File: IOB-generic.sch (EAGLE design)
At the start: 19 parts, among them J1 RJ12/6, Q0 P-FET, Q1 P-FET, Q2 P-FET, Q3 P-FET

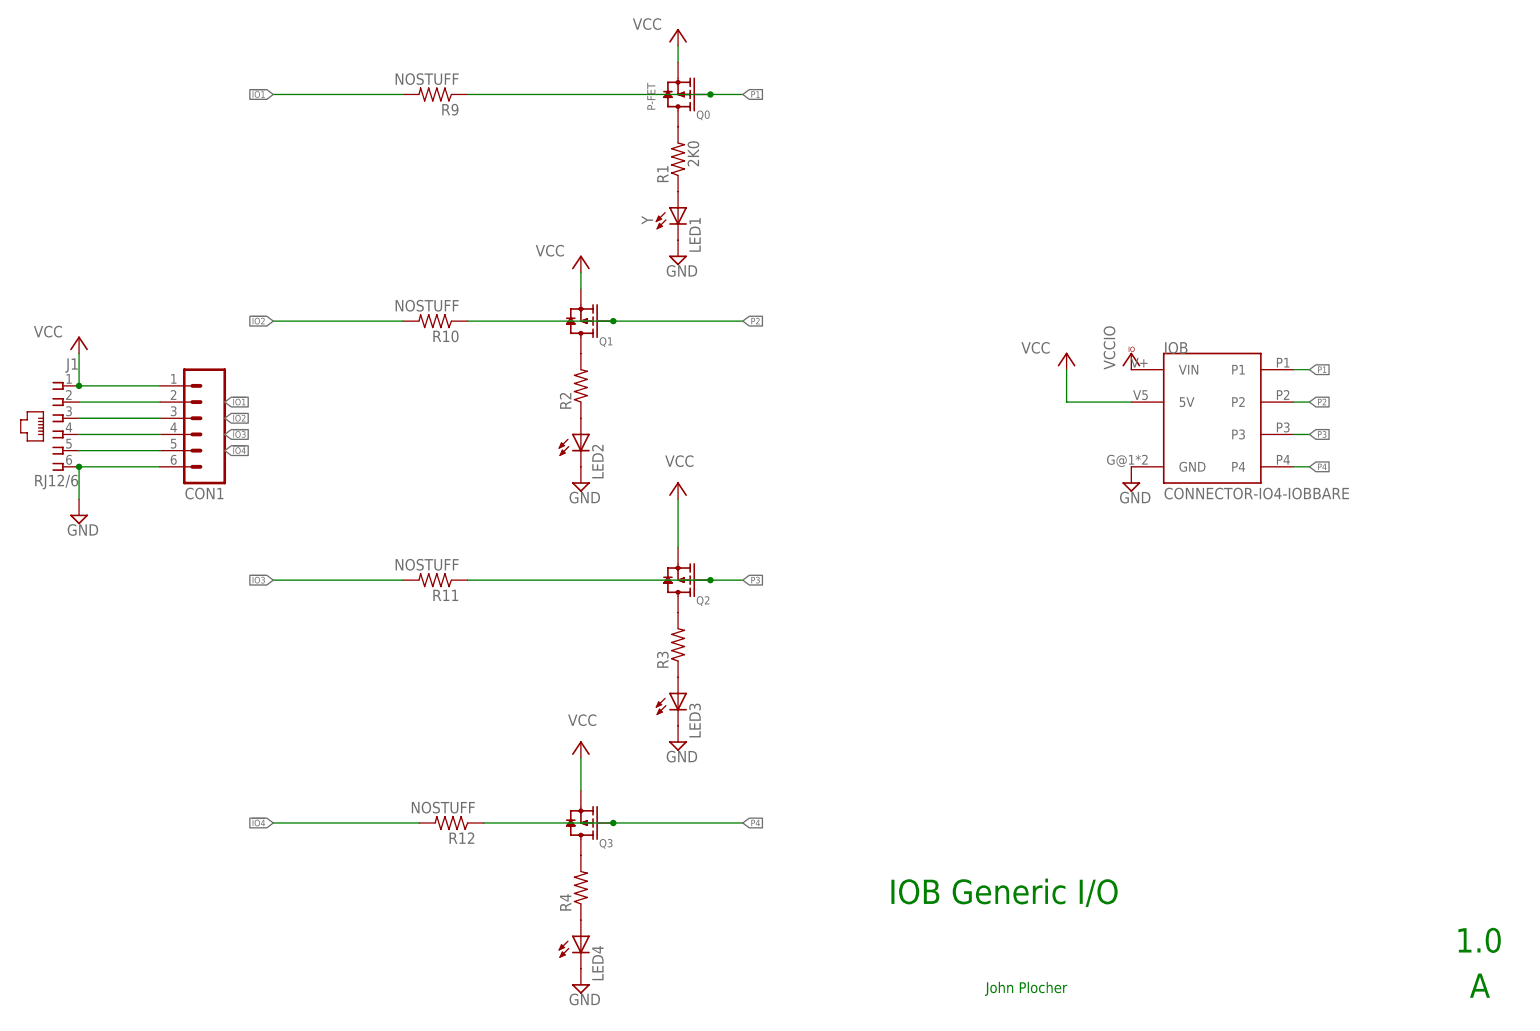
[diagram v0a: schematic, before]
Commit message: NEW IOB form factor
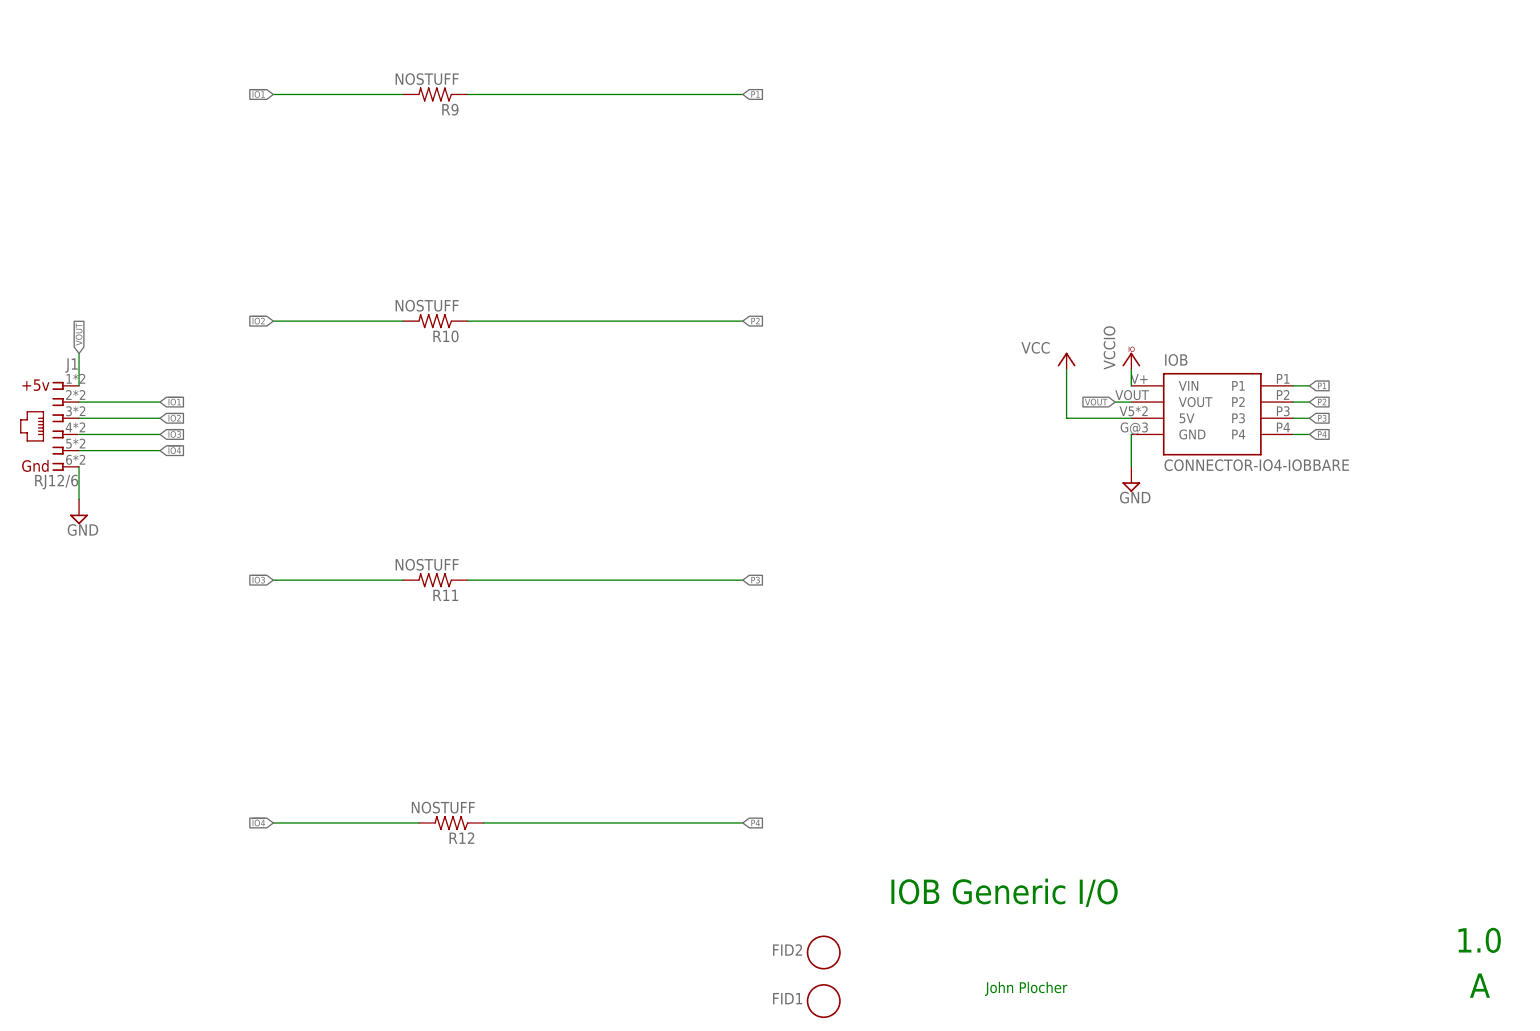
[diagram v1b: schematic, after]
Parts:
- removed CON1: (no value), SPCoast:CONNECTOR-M06LOCK
- removed LED1, LED2, LED3, LED4: Y, SPCoast:LED0603-LED
- removed Q0, Q1, Q2, Q3: P-FET, SPCoast:MOSFET-P-044021001
- removed R1, R2, R3, R4: 2K0, SPCoast:R0805-RES
- added FID1, FID2: FIDUCIAL, SPCoast:FIDUCIAL
- J1: device SPCoast:CONNECTOR-RJ25-6P6C -> SPCoast:CONNECTOR-IO4IPINS
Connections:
- removed net N$11: Q0.D, R1.2
- removed net N$2: LED1.A, R1.1
- removed net N$3: LED2.A, R2.1
- removed net N$30: Q1.D, R2.2
- removed net N$31: Q2.D, R3.2
- removed net N$32: Q3.D, R4.2
- removed net N$4: LED3.A, R3.1
- removed net N$5: LED4.A, R4.1
- new net VOUT: IOB.VOUT, J1.1
- net !IO1: no longer CON1.2
- net !IO2: no longer CON1.3
- net !IO3: no longer CON1.4
- net !IO4: no longer CON1.5
- net GND: no longer CON1.6, LED1.C, LED2.C, LED3.C, LED4.C
- net P1: no longer Q0.G
- net P2: no longer Q1.G
- net P3: no longer Q2.G
- net P4: no longer Q3.G
- net VCC: no longer CON1.1, J1.1, Q0.S, Q1.S, Q2.S, Q3.S

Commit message: updated version number
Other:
- note added: "2.0"
- note removed: "1.0"
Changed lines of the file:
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@@
 <plain>
 <text x="149.86" y="20.32" size="3.81" layer="91">IOB Generic I/O</text>
-<text x="238.76" y="12.7" size="3.81" layer="91">1.0</text>
+<text x="238.76" y="12.7" size="3.81" layer="91">2.0</text>
 <text x="241.046" y="5.588" size="3.81" layer="91">A</text>
 <text x="165.1" y="6.35" size="1.6764" layer="91" ratio="14">John Plocher</text>

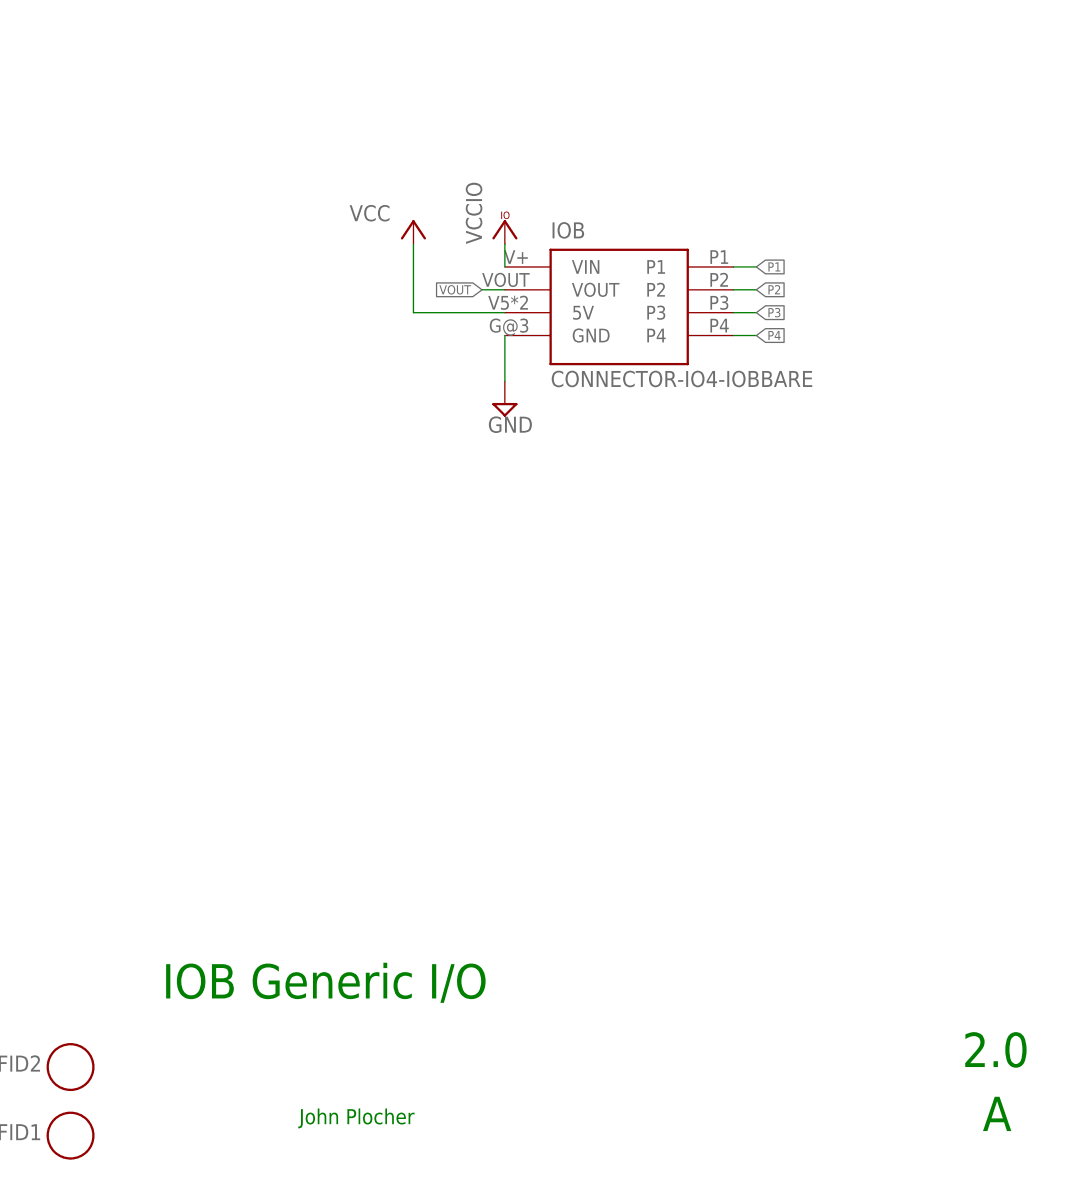
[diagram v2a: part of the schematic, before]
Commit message: silkscreen and top fill
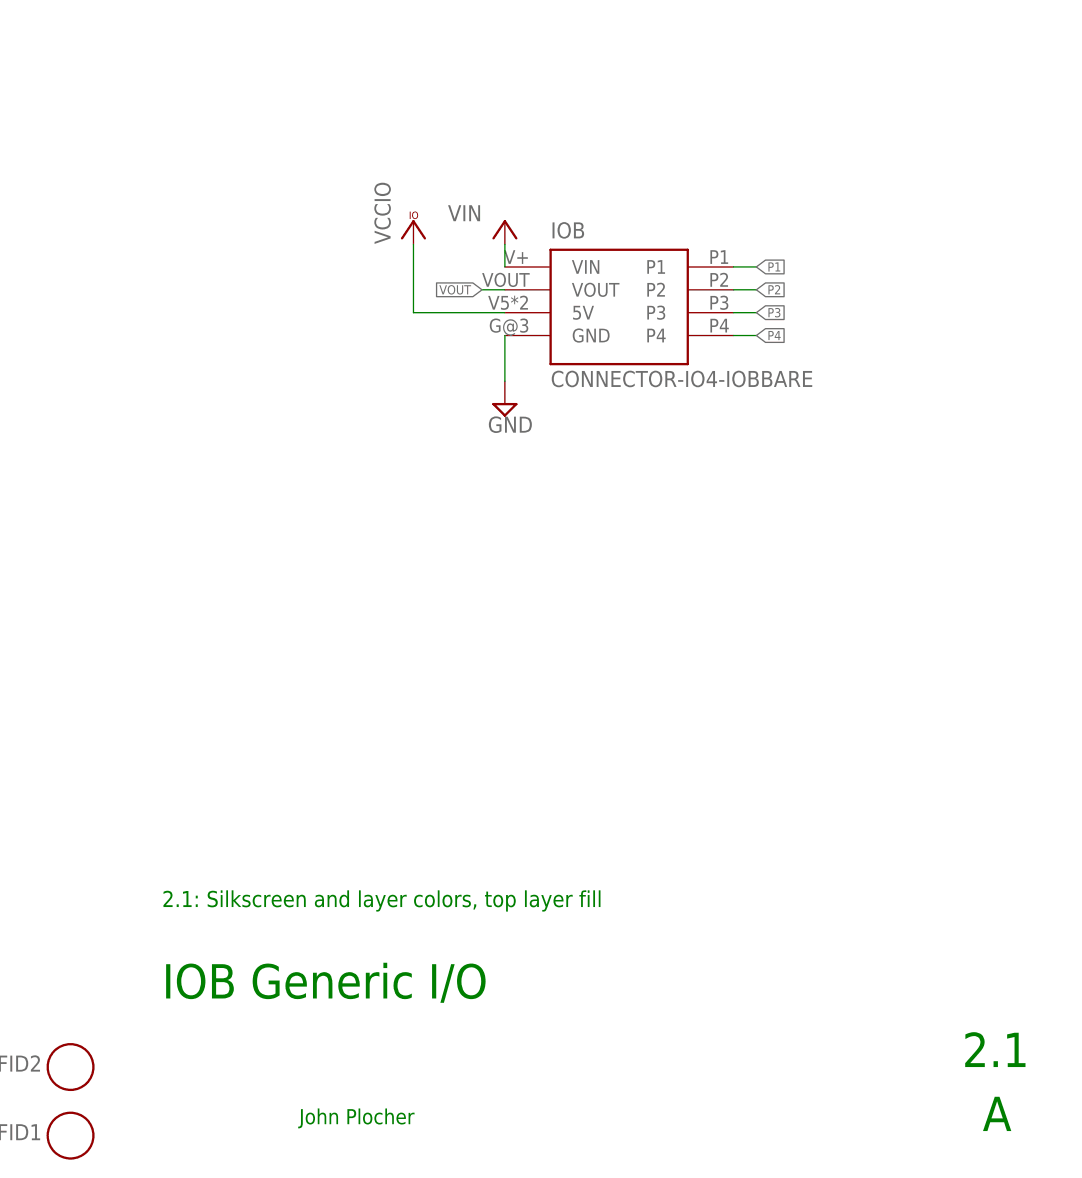
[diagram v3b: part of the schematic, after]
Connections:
- removed net VCC: IOB.5V
- new net VIN: IOB.VIN
- net VCCIO: now also IOB.5V; no longer IOB.VIN
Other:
- note added: "2.1"
- note added: "2.1: Silkscreen and layer colors, top layer fill"
- note removed: "2.0"
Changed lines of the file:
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@@
 <part name="IOB" library="SPCoast" deviceset="CONNECTOR-IO4-IOB" device="BARE"/>
 <part name="VCC3" library="SPCoast" deviceset="VCCIO" device=""/>
-<part name="P+7" library="supply1" deviceset="VCC" device=""/>
+<part name="VIN" library="supply1" deviceset="VCC" device="" value="VIN"/>
 <part name="V6" library="supply2" deviceset="GND" device=""/>
 <part name="R9" library="SPCoast" deviceset="R*" device="PTH04" value="NOSTUFF"/>
@@
 <plain>
 <text x="149.86" y="20.32" size="3.81" layer="91">IOB Generic I/O</text>
-<text x="238.76" y="12.7" size="3.81" layer="91">2.0</text>
+<text x="238.76" y="12.7" size="3.81" layer="91">2.1</text>
 <text x="241.046" y="5.588" size="3.81" layer="91">A</text>
 <text x="165.1" y="6.35" size="1.6764" layer="91" ratio="14">John Plocher</text>
+<text x="149.86" y="30.48" size="1.778" layer="91">2.1: Silkscreen and layer colors, top layer fill</text>
 </plain>
 <instances>
@@
 <instance part="V14" gate="GND" x="22.86" y="81.28"/>
 <instance part="IOB" gate="IOB" x="200.66" y="96.52"/>
-<instance part="VCC3" gate="G$1" x="187.96" y="106.68"/>
-<instance part="P+7" gate="VCC" x="177.8" y="106.68" smashed="yes" rot="MR0">
-<attribute name="VALUE" x="175.26" y="106.68" size="1.778" layer="96" rot="MR0"/>
+<instance part="VCC3" gate="G$1" x="177.8" y="106.68"/>
+<instance part="VIN" gate="VCC" x="187.96" y="106.68" smashed="yes" rot="MR0">
+<attribute name="VALUE" x="185.42" y="106.68" size="1.778" layer="96" rot="MR0"/>
 </instance>
 <instance part="V6" gate="GND" x="187.96" y="86.36"/>
@@
 <pinref part="V6" gate="GND" pin="GND"/>
 <wire x1="187.96" y1="88.9" x2="187.96" y2="93.98" width="0.1524" layer="91"/>
-</segment>
-</net>
-<net name="VCC" class="1">
-<segment>
-<pinref part="IOB" gate="IOB" pin="5V"/>
-<pinref part="P+7" gate="VCC" pin="VCC"/>
-<wire x1="187.96" y1="96.52" x2="177.8" y2="96.52" width="0.1524" layer="91"/>
-<wire x1="177.8" y1="96.52" x2="177.8" y2="104.14" width="0.1524" layer="91"/>
 </segment>
 </net>
@@
 <wire x1="213.36" y1="93.98" x2="215.9" y2="93.98" width="0.1524" layer="91"/>
 <label x="215.9" y="93.98" size="1.016" layer="95" xref="yes"/>
-</segment>
-</net>
-<net name="VCCIO" class="0">
-<segment>
-<pinref part="IOB" gate="IOB" pin="VIN"/>
-<pinref part="VCC3" gate="G$1" pin="VCCIO"/>
-<wire x1="187.96" y1="104.14" x2="187.96" y2="101.6" width="0.1524" layer="91"/>
 </segment>
 </net>
@@
 </segment>
 </net>
+<net name="VCCIO" class="1">
+<segment>
+<pinref part="IOB" gate="IOB" pin="5V"/>
+<wire x1="187.96" y1="96.52" x2="177.8" y2="96.52" width="0.1524" layer="91"/>
+<wire x1="177.8" y1="96.52" x2="177.8" y2="104.14" width="0.1524" layer="91"/>
+<pinref part="VCC3" gate="G$1" pin="VCCIO"/>
+</segment>
+</net>
+<net name="VIN" class="0">
+<segment>
+<pinref part="VIN" gate="VCC" pin="VCC"/>
+<pinref part="IOB" gate="IOB" pin="VIN"/>
+<wire x1="187.96" y1="104.14" x2="187.96" y2="101.6" width="0.1524" layer="91"/>
+</segment>
+</net>

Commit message: silkscreen and top fill, array
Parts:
- IOB: value CONNECTOR-IO4-IOBBARE -> CONNECTOR-IO4-IOBFULL; device SPCoast:CONNECTOR-IO4-IOBBARE -> SPCoast:CONNECTOR-IO4-IOBFULL
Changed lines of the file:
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@@
 <part name="J1" library="SPCoast" deviceset="CONNECTOR-IO4" device="IPINS" value="RJ12/6"/>
 <part name="V14" library="supply2" deviceset="GND" device=""/>
-<part name="IOB" library="SPCoast" deviceset="CONNECTOR-IO4-IOB" device="BARE"/>
+<part name="IOB" library="SPCoast" deviceset="CONNECTOR-IO4-IOB" device="FULL"/>
 <part name="VCC3" library="SPCoast" deviceset="VCCIO" device=""/>
 <part name="VIN" library="supply1" deviceset="VCC" device="" value="VIN"/>
